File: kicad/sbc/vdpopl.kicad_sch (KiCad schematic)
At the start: 24 parts, among them U1 74LS139, U2 V9958, U3 DRAM_64KX4, U4 DRAM_64KX4, U5 DRAM_64KX4, U6 DRAM_64KX4, U7 DRAM_64KX4, U8 YM3812, U9 DRAM_64KX4, Y1 21,443Mhz

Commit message: complete schematics
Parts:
- U1: footprint Package_DIP:DIP-16_W7.62mm_Socket_LongPads -> Package_DIP:DIP-16_W7.62mm_LongPads
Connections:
- net Audio_analog/LOAD: now reaches U8.20 (SH)
- net Audio_analog/SD: now reaches U8.21 (MO)
- net Audio_analog/fl: now reaches U8.23 (fSY)
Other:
- added sheet Audio_analog (a_analog.kicad_sch)
- added sheet Video_analog (v_analog.kicad_sch)
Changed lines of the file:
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@@
     (stroke (width 0) (type default))
   )
-  (wire (pts (xy 153.67 93.98) (xy 161.29 93.98))
+  (wire (pts (xy 153.67 93.98) (xy 196.85 93.98))
     (stroke (width 0) (type default))
   )
@@
     (stroke (width 0) (type default))
   )
+  (wire (pts (xy 190.5 120.65) (xy 190.5 109.22))
+    (stroke (width 0) (type default))
+  )
   (wire (pts (xy 173.99 33.02) (xy 177.8 33.02))
     (stroke (width 0) (type default))
@@
     (stroke (width 0) (type default))
   )
-  (wire (pts (xy 153.67 101.6) (xy 161.29 101.6))
+  (wire (pts (xy 153.67 101.6) (xy 196.85 101.6))
     (stroke (width 0) (type default))
   )
@@
     (stroke (width 0) (type default))
   )
-  (wire (pts (xy 153.67 99.06) (xy 161.29 99.06))
+  (wire (pts (xy 153.67 99.06) (xy 196.85 99.06))
     (stroke (width 0) (type default))
   )
@@
     (stroke (width 0) (type default))
   )
+  (wire (pts (xy 190.5 109.22) (xy 196.85 109.22))
+    (stroke (width 0) (type default))
+  )
   (wire (pts (xy 156.21 29.21) (xy 153.67 29.21))
     (stroke (width 0) (type default))
@@
     (stroke (width 0) (type default))
   )
-  (wire (pts (xy 153.67 96.52) (xy 161.29 96.52))
+  (wire (pts (xy 153.67 96.52) (xy 196.85 96.52))
     (stroke (width 0) (type default))
   )
@@
   )
   (wire (pts (xy 129.54 21.59) (xy 129.54 13.97))
+    (stroke (width 0) (type default))
+  )
+  (wire (pts (xy 186.69 120.65) (xy 190.5 120.65))
     (stroke (width 0) (type default))
   )
@@
       (effects (font (size 1.27 1.27)))
     )
-    (property "Footprint" "Package_DIP:DIP-16_W7.62mm_Socket_LongPads" (at 67.31 97.79 0)
+    (property "Footprint" "Package_DIP:DIP-16_W7.62mm_LongPads" (at 67.31 97.79 0)
       (effects (font (size 1.27 1.27)) hide)
     )
@@
       (effects (font (size 1.27 1.27)))
     )
-    (property "Footprint" "Package_DIP:DIP-16_W7.62mm_Socket_LongPads" (at 67.31 72.39 0)
+    (property "Footprint" "Package_DIP:DIP-16_W7.62mm_LongPads" (at 67.31 72.39 0)
       (effects (font (size 1.27 1.27)) hide)
     )
@@
       )
     )
+  )
+  (sheet (at 196.85 90.17) (size 25.4 21.59) (fields_autoplaced)
+    (stroke (width 0.1524) (type solid))
+    (fill (color 0 0 0 0.0000))
+    (property "Sheetname" "Video_analog" (at 196.85 89.4584 0)
+      (effects (font (size 1.27 1.27)) (justify left bottom))
+    )
+    (property "Sheetfile" "v_analog.kicad_sch" (at 196.85 112.3446 0)
+      (effects (font (size 1.27 1.27)) (justify left top))
+    )
+    (property "Field2" "" (at 196.85 90.17 0)
+      (effects (font (size 1.27 1.27)) hide)
+    )
+    (pin "AUDIO_OUT" input (at 196.85 109.22 180)
+      (effects (font (size 1.27 1.27)) (justify left))
+    )
+    (pin "RGB_G" input (at 196.85 99.06 180)
+      (effects (font (size 1.27 1.27)) (justify left))
+    )
+    (pin "CSYNC" input (at 196.85 101.6 180)
+      (effects (font (size 1.27 1.27)) (justify left))
+    )
+    (pin "RGB_R" input (at 196.85 96.52 180)
+      (effects (font (size 1.27 1.27)) (justify left))
+    )
+    (pin "RGB_B" input (at 196.85 93.98 180)
+      (effects (font (size 1.27 1.27)) (justify left))
+    )
+    (instances
+      (project "sbc"
+        (path "/896d5dab-44ec-47d0-8232-7ef57773545e/28a4b651-8375-4e62-9061-4149cd570bf0" (page "6"))
+      )
+    )
+  )
+  (sheet (at 162.56 114.3) (size 24.13 16.51) (fields_autoplaced)
+    (stroke (width 0.1524) (type solid))
+    (fill (color 0 0 0 0.0000))
+    (property "Sheetname" "Audio_analog" (at 162.56 113.5884 0)
+      (effects (font (size 1.27 1.27)) (justify left bottom))
+    )
+    (property "Sheetfile" "a_analog.kicad_sch" (at 162.56 131.3946 0)
+      (effects (font (size 1.27 1.27)) (justify left top))
+    )
+    (pin "LOAD" input (at 162.56 120.65 180)
+      (effects (font (size 1.27 1.27)) (justify left))
+    )
+    (pin "SD" input (at 162.56 123.19 180)
+      (effects (font (size 1.27 1.27)) (justify left))
+    )
+    (pin "fl" input (at 162.56 118.11 180)
+      (effects (font (size 1.27 1.27)) (justify left))
+    )
+    (pin "AUDIO_OUT" output (at 186.69 120.65 0)
+      (effects (font (size 1.27 1.27)) (justify right))
+    )
+    (instances
+      (project "sbc"
+        (path "/896d5dab-44ec-47d0-8232-7ef57773545e/28a4b651-8375-4e62-9061-4149cd570bf0" (page "5"))
+      )
+    )

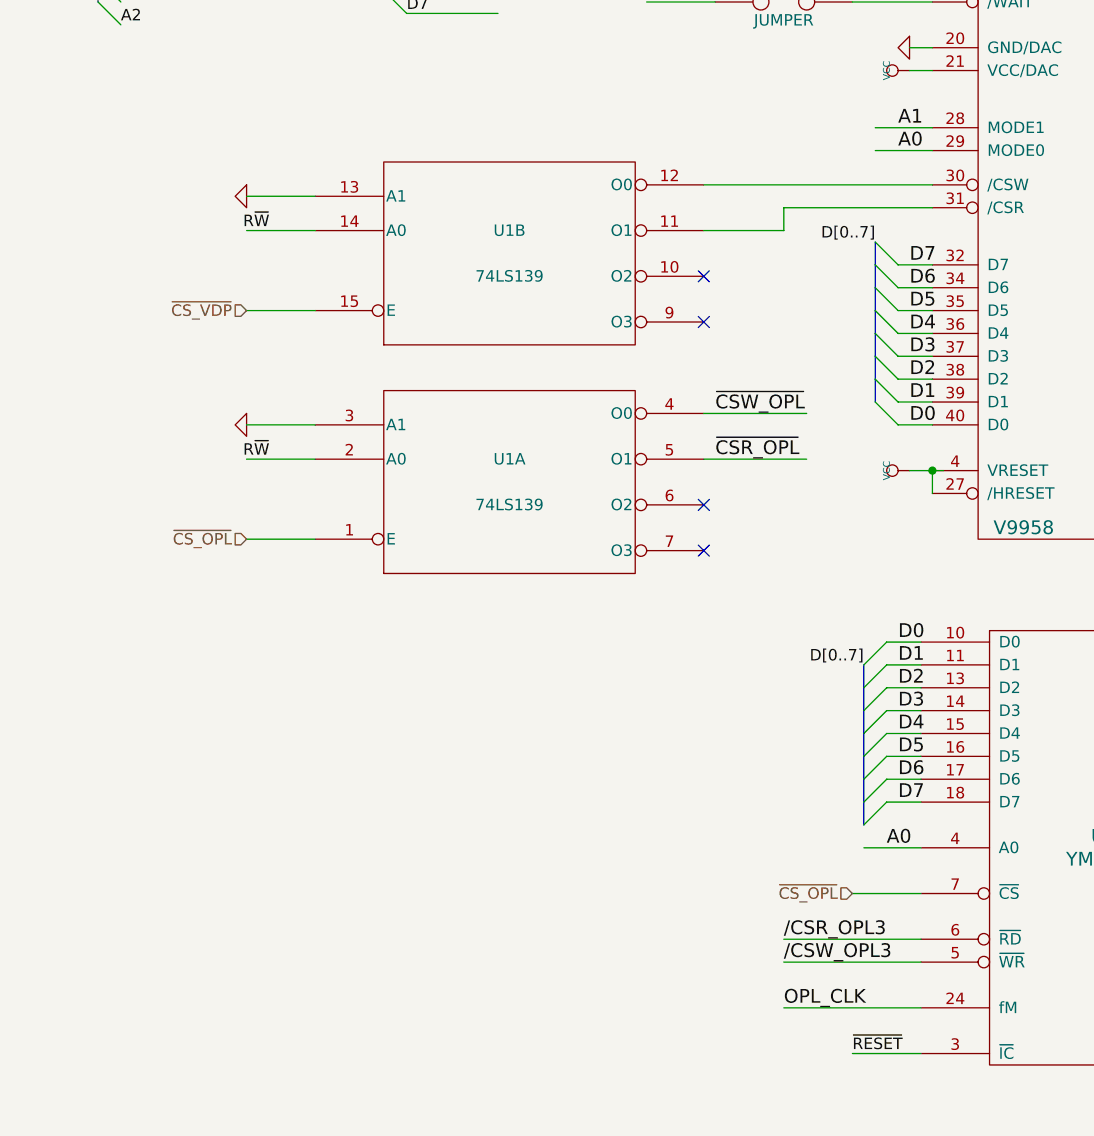
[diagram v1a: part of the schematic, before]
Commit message: removed U17
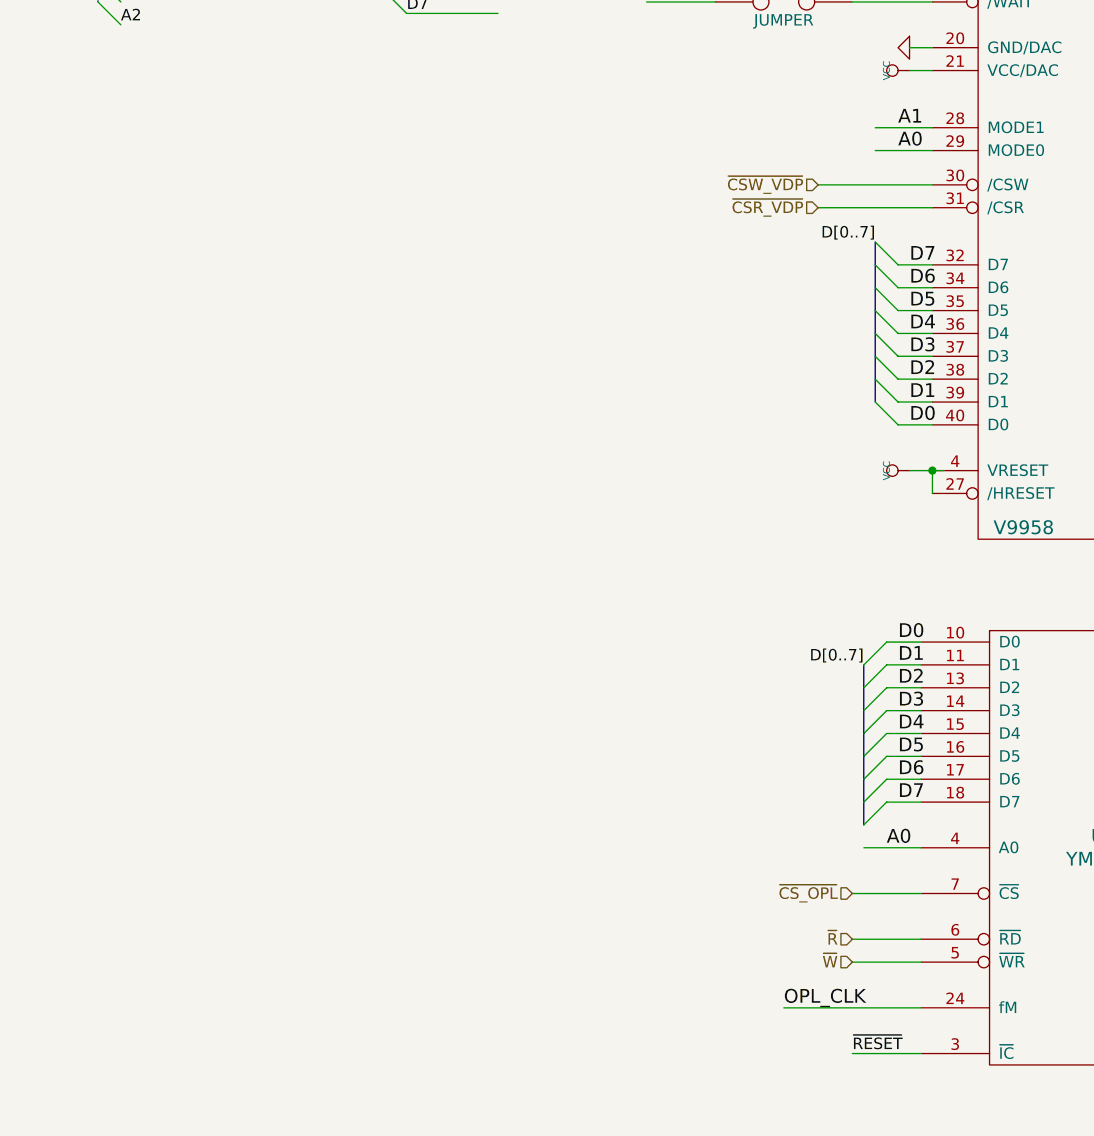
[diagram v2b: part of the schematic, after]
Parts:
- removed U1: 74LS139, Package_DIP:DIP-16_W7.62mm_LongPads, symbol v9958-rescue:74LS139
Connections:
- net ~{CSW_VDP}: now reaches U2.30 (/CSW)
- net ~{CSR_VDP}: now reaches U2.31 (/CSR)
- net /CSR_OPL3 renamed ~{R}
- net /CSW_OPL3 renamed ~{W}
- no-connect marks 5 -> 1

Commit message: fix ERC messages
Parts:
- C1, C10, C2, C28, C29, C3, C4, C5, C6, C7, C8, C9: symbol v9958-rescue:C -> Device:C
- C30: symbol v9958-rescue:CP -> Device:C_Polarized
- JP1: symbol v9958-rescue:JUMPER -> Jumper:Jumper_2_Open
- U2: symbol v9958-rescue:V9958 -> tms99x:V9958
- U3, U4, U5, U6, U7, U9: symbol v9958-rescue:DRAM_64KX4 -> dram:DRAM_64KX4
- U8: symbol v9958-rescue:YM3812 -> yamaha_opl:YM3812
- Y1: symbol v9958-rescue:Crystal_Small -> Device:Crystal_Small
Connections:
- net RD4: no longer U2.45 (RD4), U4.2 (DQ0)
- net R/W renamed VDP_R~{W}
- new net VDP_RD4: U2.45 (RD4), U4.2 (DQ0)
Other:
- moved on the sheet: C1, C2, JP1, U2, U8, Y1

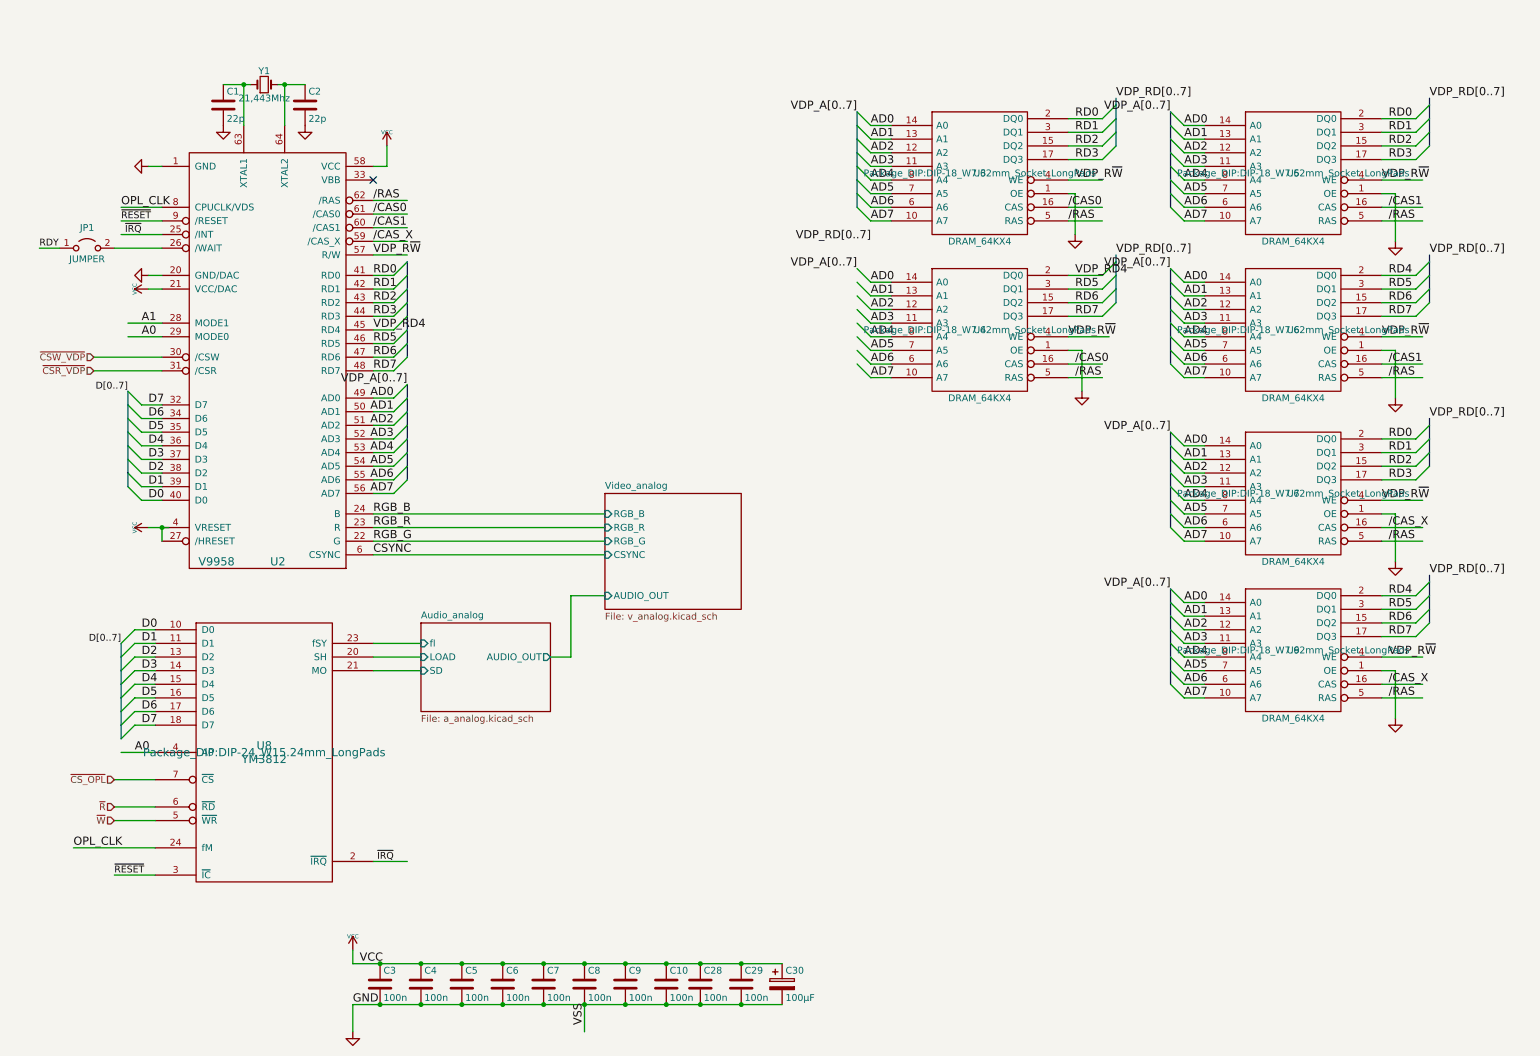
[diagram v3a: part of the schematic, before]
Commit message: cleanup ERC warnings and errors
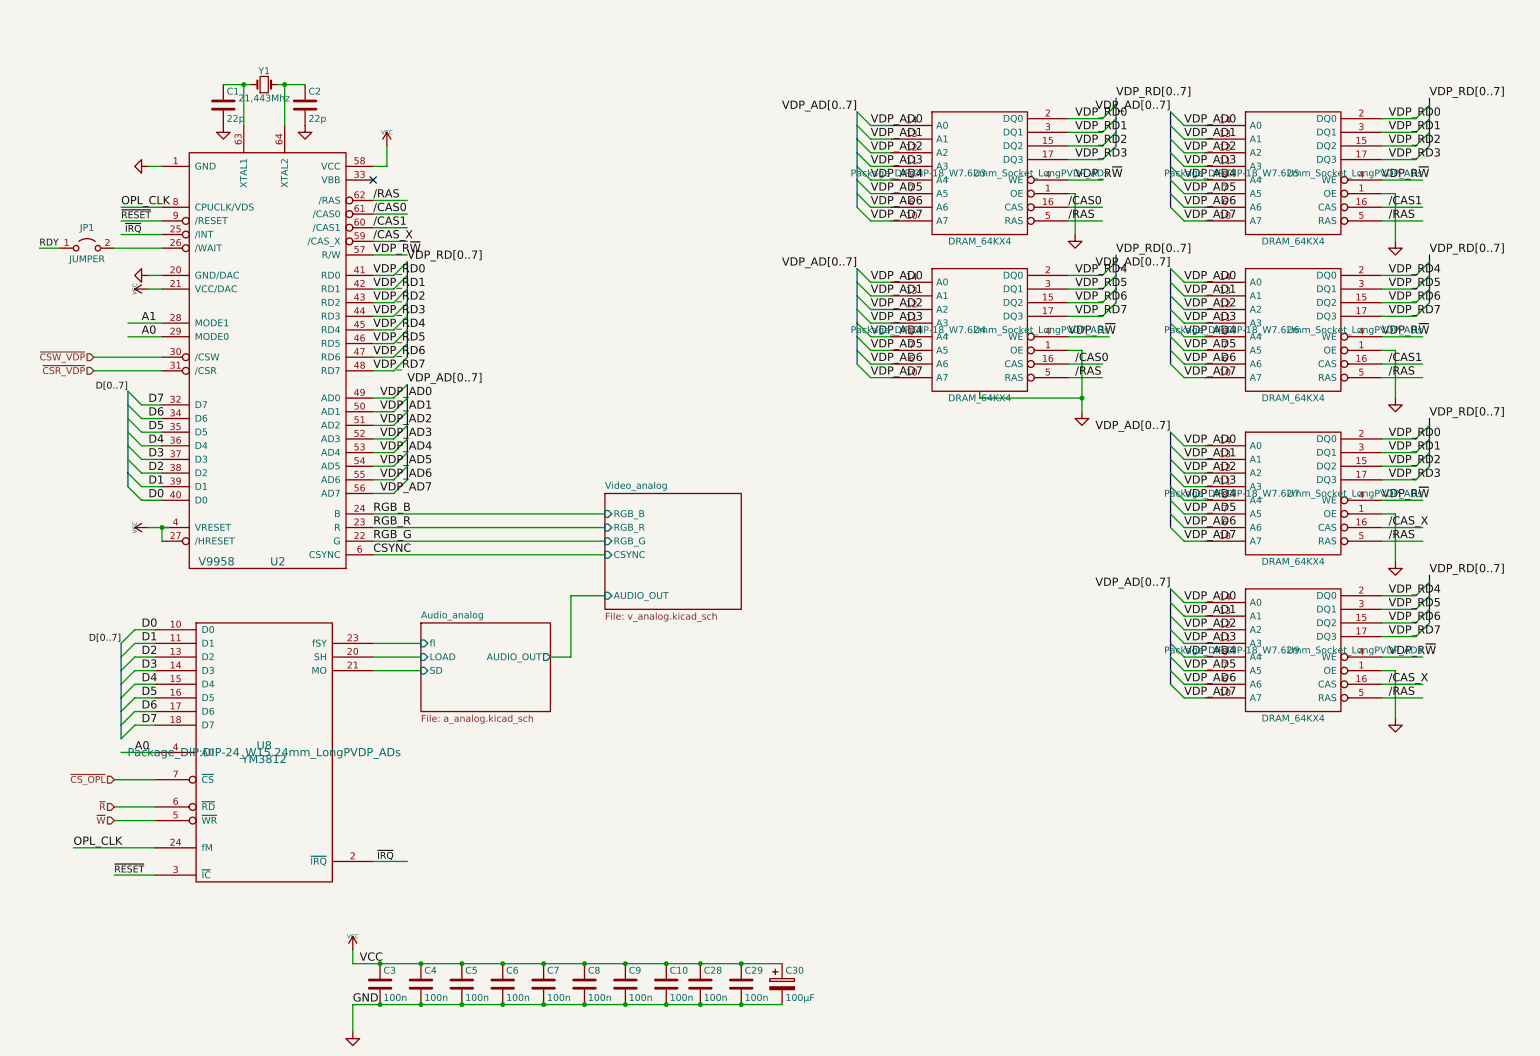
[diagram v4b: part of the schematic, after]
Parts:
- U3, U4, U5, U6, U7, U9: footprint Package_DIP:DIP-18_W7.62mm_Socket_LongPads -> Package_DIP:DIP-18_W7.62mm_Socket_LongPVDP_ADs
- U8: footprint Package_DIP:DIP-24_W15.24mm_LongPads -> Package_DIP:DIP-24_W15.24mm_LongPVDP_ADs
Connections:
- net RD4 is gone; now on net VDP_RD4: U6.2 (DQ0), U9.2 (DQ0)
- net AD0 renamed VDP_AD0
- net AD1 renamed VDP_AD1
- net AD2 renamed VDP_AD2
- net AD3 renamed VDP_AD3
- net AD4 renamed VDP_AD4
- net AD5 renamed VDP_AD5
- net AD6 renamed VDP_AD6
- net AD7 renamed VDP_AD7
- net RD0 renamed VDP_RD0
- net RD1 renamed VDP_RD1
- net RD2 renamed VDP_RD2
- net RD3 renamed VDP_RD3
- net RD5 renamed VDP_RD5
- net RD6 renamed VDP_RD6
- net RD7 renamed VDP_RD7
